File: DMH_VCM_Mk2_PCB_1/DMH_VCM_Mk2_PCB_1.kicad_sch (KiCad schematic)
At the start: 0 parts

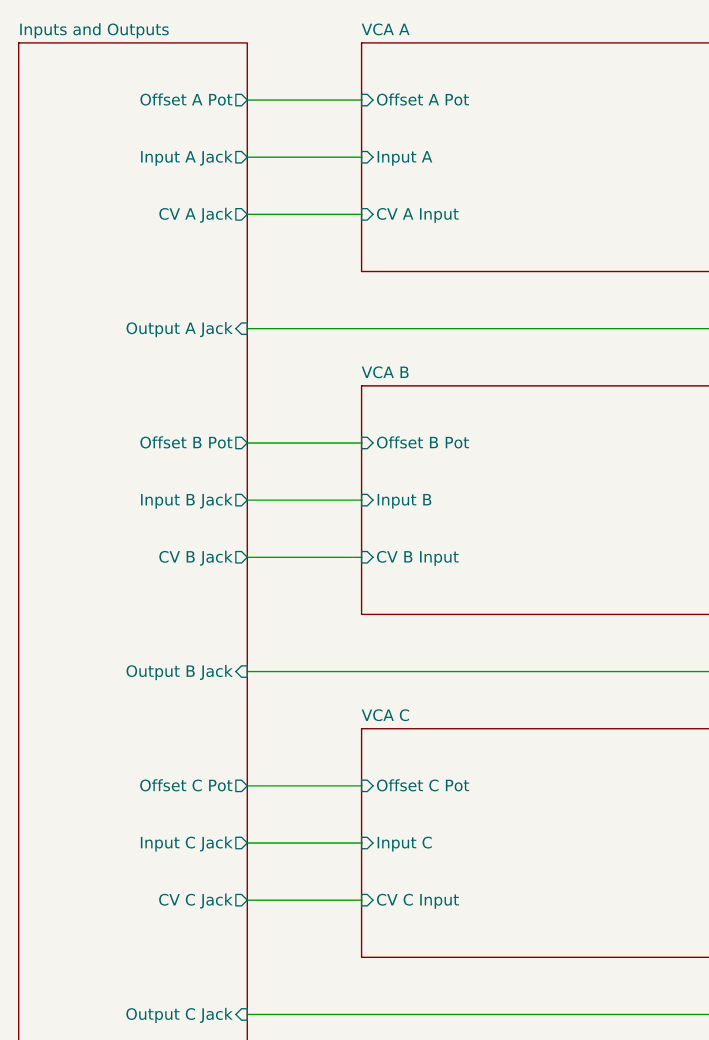
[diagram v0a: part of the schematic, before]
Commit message: Almost finished PCB 1 schematic
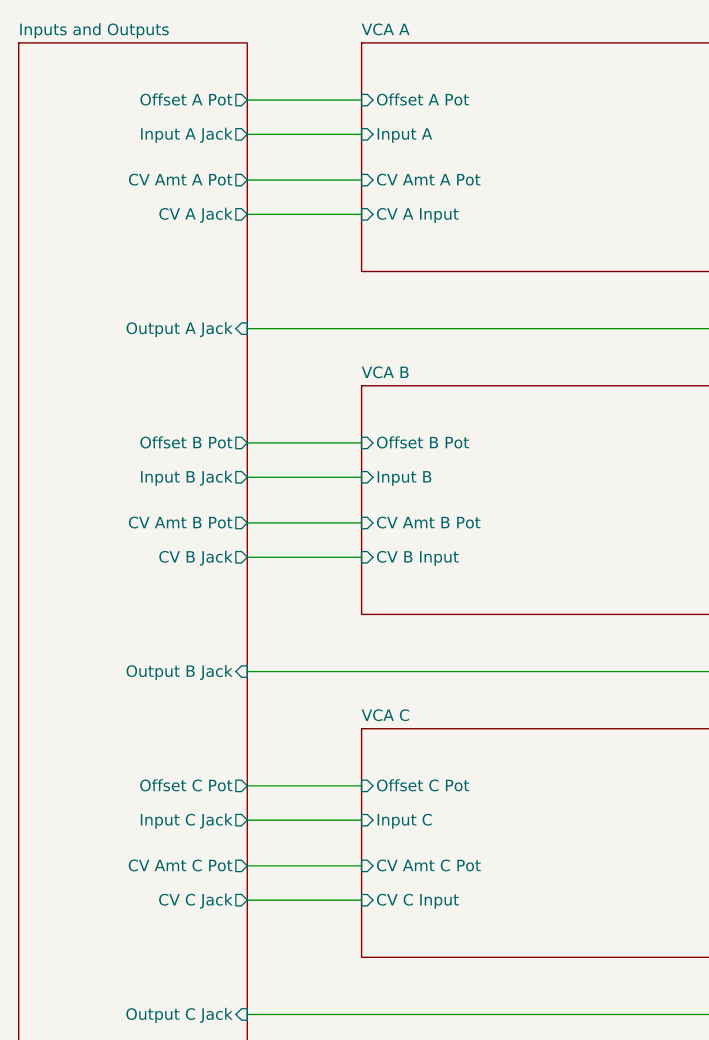
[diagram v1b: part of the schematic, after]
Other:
- sheet Inputs and Outputs ports: added CV Amt A Pot, CV Amt B Pot, CV Amt C Pot; removed none
- sheet VCA A ports: added CV Amt A Pot; removed none
- sheet VCA B ports: added CV Amt B Pot; removed none
- sheet VCA C ports: added CV Amt C Pot; removed none
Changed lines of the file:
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@@
+	(wire
+		(pts
+			(xy 50.8 78.74) (xy 63.5 78.74)
+		)
+		(stroke
+			(width 0)
+			(type default)
+		)
+	)
 	(wire
 		(pts
@@
 	(wire
 		(pts
-			(xy 50.8 38.1) (xy 63.5 38.1)
-		)
-		(stroke
-			(width 0)
-			(type default)
-		)
-	)
-	(wire
-		(pts
-			(xy 50.8 76.2) (xy 63.5 76.2)
+			(xy 50.8 35.56) (xy 63.5 35.56)
+		)
+		(stroke
+			(width 0)
+			(type default)
+		)
+	)
+	(wire
+		(pts
+			(xy 50.8 73.66) (xy 63.5 73.66)
 		)
 		(stroke
@@
 	(wire
 		(pts
+			(xy 50.8 40.64) (xy 63.5 40.64)
+		)
+		(stroke
+			(width 0)
+			(type default)
+		)
+	)
+	(wire
+		(pts
 			(xy 50.8 57.15) (xy 127 57.15)
 		)
@@
 	(wire
 		(pts
+			(xy 50.8 116.84) (xy 63.5 116.84)
+		)
+		(stroke
+			(width 0)
+			(type default)
+		)
+	)
+	(wire
+		(pts
 			(xy 50.8 158.75) (xy 63.5 158.75)
 		)
@@
 	(wire
 		(pts
-			(xy 50.8 114.3) (xy 63.5 114.3)
+			(xy 50.8 111.76) (xy 63.5 111.76)
 		)
 		(stroke
@@
 		)
 		(instances
-			(project "DMH_Tripple_VCA_PCB_1"
+			(project "DMH_VCM_Mk2_PCB_1"
 				(path "/58f4306d-5387-4983-bb08-41a2313fd315"
 					(page "4")
@@
 		)
 		(pin "Input A" input
-			(at 63.5 38.1 180)
+			(at 63.5 35.56 180)
 			(effects
 				(font
@@
 			)
 		)
+		(pin "CV Amt A Pot" input
+			(at 63.5 40.64 180)
+			(effects
+				(font
+					(size 1.27 1.27)
+				)
+				(justify left)
+			)
+		)
 		(instances
-			(project "DMH_Tripple_VCA_PCB_1"
+			(project "DMH_VCM_Mk2_PCB_1"
 				(path "/58f4306d-5387-4983-bb08-41a2313fd315"
 					(page "3")
@@
 		)
 		(pin "Input B" input
-			(at 63.5 76.2 180)
+			(at 63.5 73.66 180)
 			(effects
 				(font
@@
 			)
 		)
+		(pin "CV Amt B Pot" input
+			(at 63.5 78.74 180)
+			(effects
+				(font
+					(size 1.27 1.27)
+				)
+				(justify left)
+			)
+		)
 		(instances
-			(project "DMH_Tripple_VCA_PCB_1"
+			(project "DMH_VCM_Mk2_PCB_1"
 				(path "/58f4306d-5387-4983-bb08-41a2313fd315"
 					(page "5")
@@
 		)
 		(pin "Input B Jack" output
-			(at 50.8 76.2 0)
+			(at 50.8 73.66 0)
 			(effects
 				(font
@@
 		)
 		(pin "Input C Jack" output
-			(at 50.8 114.3 0)
+			(at 50.8 111.76 0)
 			(effects
 				(font
@@
 		)
 		(pin "Input A Jack" output
-			(at 50.8 38.1 0)
+			(at 50.8 35.56 0)
 			(effects
 				(font
@@
 			)
 		)
+		(pin "CV Amt A Pot" output
+			(at 50.8 40.64 0)
+			(effects
+				(font
+					(size 1.27 1.27)
+				)
+				(justify right)
+			)
+		)
+		(pin "CV Amt B Pot" output
+			(at 50.8 78.74 0)
+			(effects
+				(font
+					(size 1.27 1.27)
+				)
+				(justify right)
+			)
+		)
+		(pin "CV Amt C Pot" output
+			(at 50.8 116.84 0)
+			(effects
+				(font
+					(size 1.27 1.27)
+				)
+				(justify right)
+			)
+		)
 		(instances
-			(project "DMH_Tripple_VCA_PCB_1"
+			(project "DMH_VCM_Mk2_PCB_1"
 				(path "/58f4306d-5387-4983-bb08-41a2313fd315"
 					(page "2")
@@
 		)
 		(instances
-			(project "DMH_Tripple_VCA_PCB_1"
+			(project "DMH_VCM_Mk2_PCB_1"
 				(path "/58f4306d-5387-4983-bb08-41a2313fd315"
 					(page "7")
@@
 		)
 		(pin "Input C" input
-			(at 63.5 114.3 180)
+			(at 63.5 111.76 180)
 			(effects
 				(font
@@
 			)
 		)
+		(pin "CV Amt C Pot" input
+			(at 63.5 116.84 180)
+			(effects
+				(font
+					(size 1.27 1.27)
+				)
+				(justify left)
+			)
+		)
 		(instances
-			(project "DMH_Tripple_VCA_PCB_1"
+			(project "DMH_VCM_Mk2_PCB_1"
 				(path "/58f4306d-5387-4983-bb08-41a2313fd315"
 					(page "6")
